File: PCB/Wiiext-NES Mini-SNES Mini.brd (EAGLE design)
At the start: 58.5 x 61 mm, 16 parts, among them J1 USB4085-GF-A_REVA4

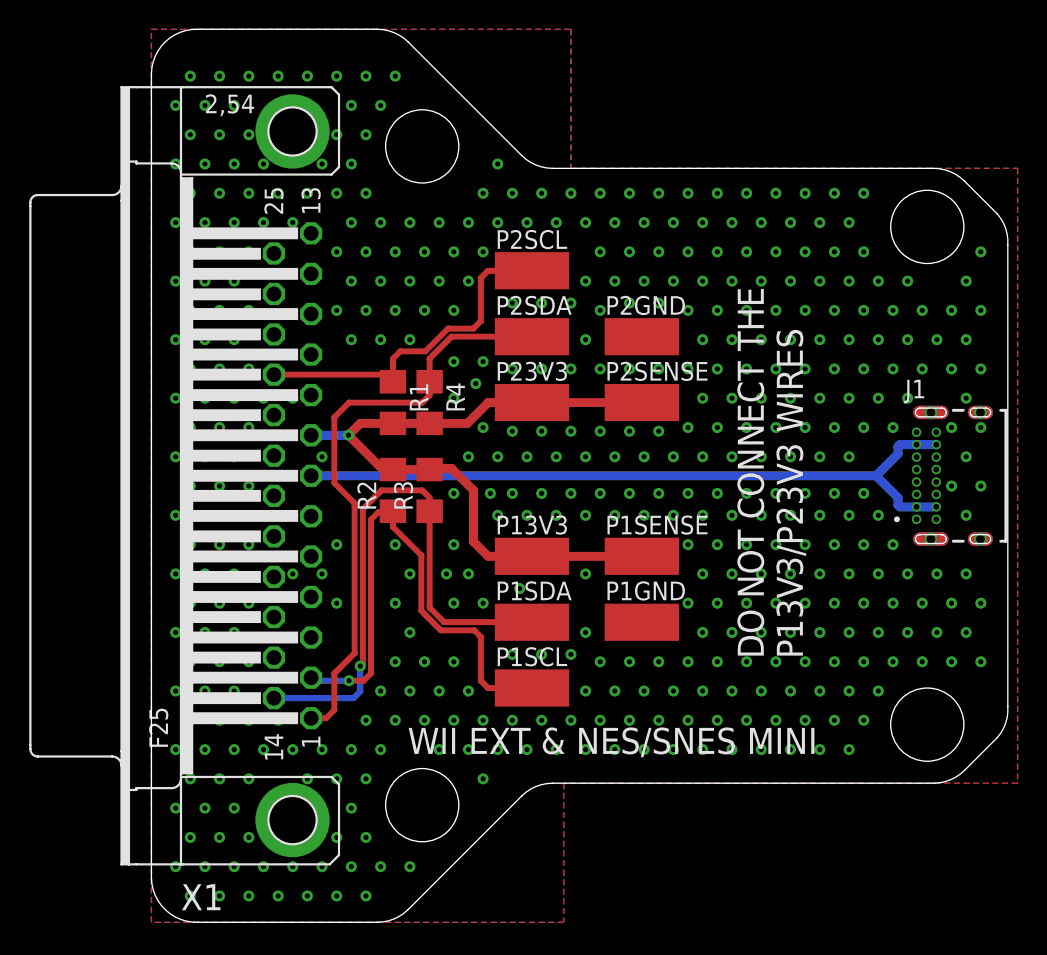
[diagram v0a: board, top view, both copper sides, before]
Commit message: Add Support for 5V PD Chargers (#61)
Added 5.1K pull down resistors on the CC1 and CC2 to enable the use of a PD charger for 5V charging.  Also cleaned up the PCB design and spread out pads for easier assembly.
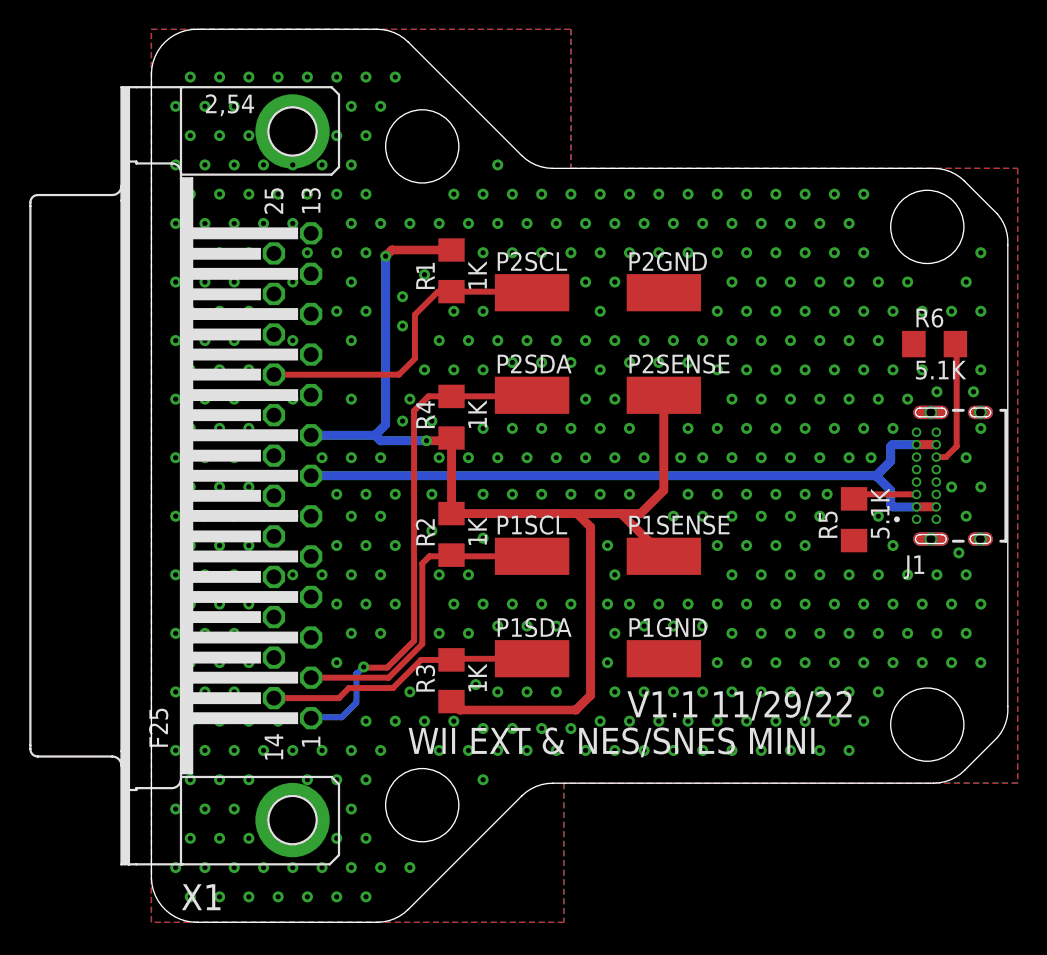
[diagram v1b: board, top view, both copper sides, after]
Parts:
- removed P13V3, P23V3: (no value), wirepad:SMD2,54-5,08
- added R5, R6: 5.1K, adafruit:R1206
- moved R3 13.1 mm to (20.5, 16.5), turned to 270 degrees
- moved R1 9.85 mm to (20.5, 44.5), turned to 90 degrees
- moved P1SCL 9.00 mm to (26.0, 25.0)
- moved R2 5.00 mm to (20.5, 26.5)
- moved P2SDA 4.00 mm to (26.0, 36.0)
- moved P2GND 3.35 mm to (35.0, 43.0)
- moved P1GND 2.92 mm to (35.0, 18.0)
- moved P1SDA 2.50 mm to (26.0, 18.0)
- moved R4 1.80 mm to (20.5, 34.5)
- moved P2SENSE 1.58 mm to (35.0, 36.0)
- moved P1SENSE 1.50 mm to (35.0, 25.0)
- moved P2SCL 1.50 mm to (26.0, 43.0)
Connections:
- new net PD1: J1.B5, R6.2
- new net PD2: J1.A5, R5.2
- net 3V3IN: no longer P13V3.1, P23V3.1
- net GND: now also J1.S1, J1.S2, J1.S3, J1.S4, R5.1, R6.1
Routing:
- net 3V3IN: track 49.1 -> 80.9 mm, vias 1 -> 2
- net IO26: track 38.8 -> 18.7 mm, vias 1 -> 0
- net IO25: track 35.7 -> 21.9 mm, vias 1 -> 0
- net PD1: track 0.00 -> 8.72 mm
- net IO27: track 40.3 -> 34.6 mm, vias 0 -> 1
- net PD2: track 0.00 -> 4.39 mm
- net 5VIN: track 49.2 -> 49.8 mm
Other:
- board text added: "V1.1 11/29/22"
- board text removed: "DO NOT CONNECT THE P13V3/P23V3 WIRES"
- board text removed: "V1.0 11/14/22"
